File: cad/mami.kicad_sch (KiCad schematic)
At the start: 130 parts, among them J1 Conn_01x02_Pin, SW1 SW_Push, SW10 SW_Push, SW11 SW_Push, SW12 SW_Push, SW13 SW_Push, SW14 SW_Push, SW15 SW_Push, SW16 SW_Push, SW17 SW_Push, SW18 SW_Push, SW19 SW_Push, SW2 SW_Push, SW20 SW_Push, SW21 SW_Push, SW22 SW_Push, SW23 SW_Push, SW24 SW_Push, SW25 SW_Push, SW26 SW_Push, SW27 SW_Push, SW28 SW_Push, SW29 SW_Push, SW3 SW_Push, SW30 SW_Push, SW31 SW_Push, SW32 SW_Push, SW33 SW_Push, SW34 SW_Push, SW35 SW_Push, SW36 SW_Push, SW37 SW_Push, SW38 SW_Push, SW39 SW_Push, SW4 SW_Push, SW40 SW_Push, SW41 SW_Push, SW42 SW_Push, SW43 ResetSW, SW45 SW_SPDT, SW5 SW_Push, SW6 SW_Push, SW7 SW_Push, SW8 SW_Push, SW9 SW_Push, U1 nice_nano

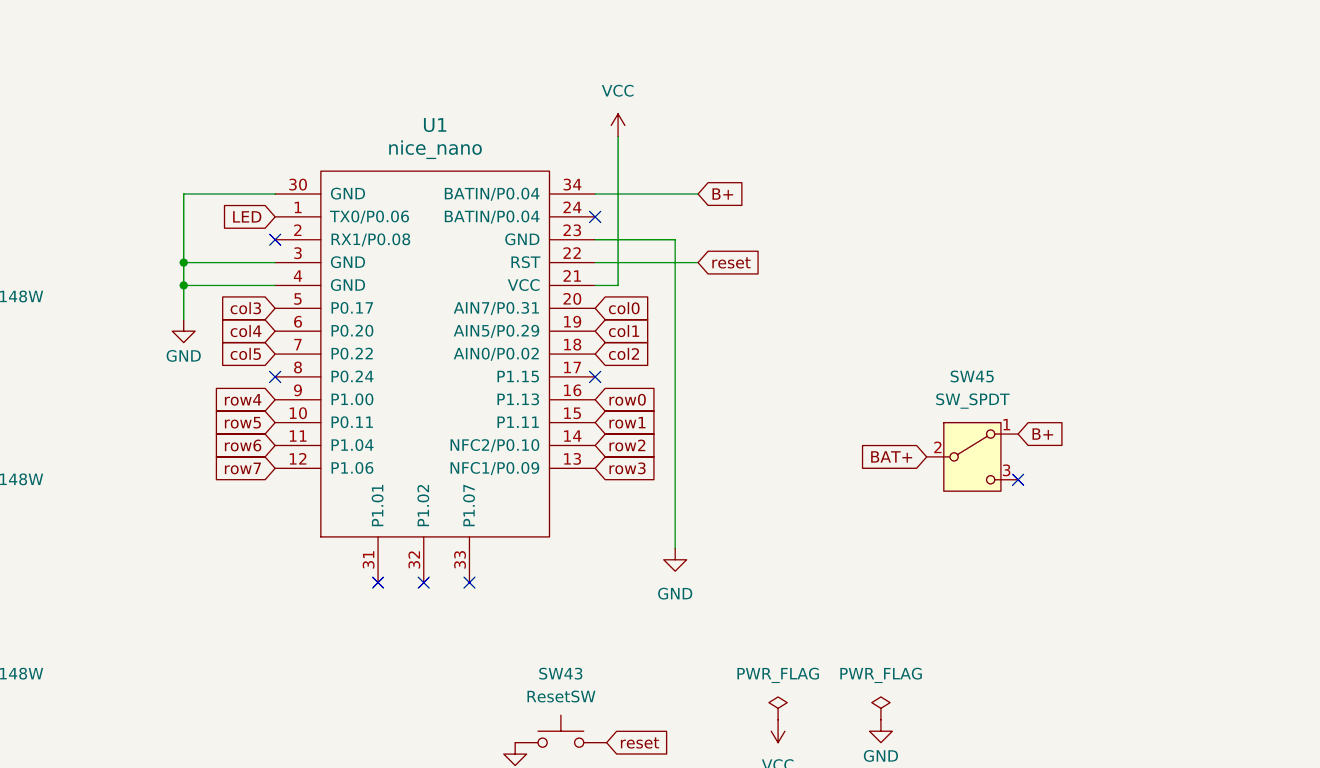
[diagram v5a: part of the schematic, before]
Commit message: ON/OFFスイッチを削除
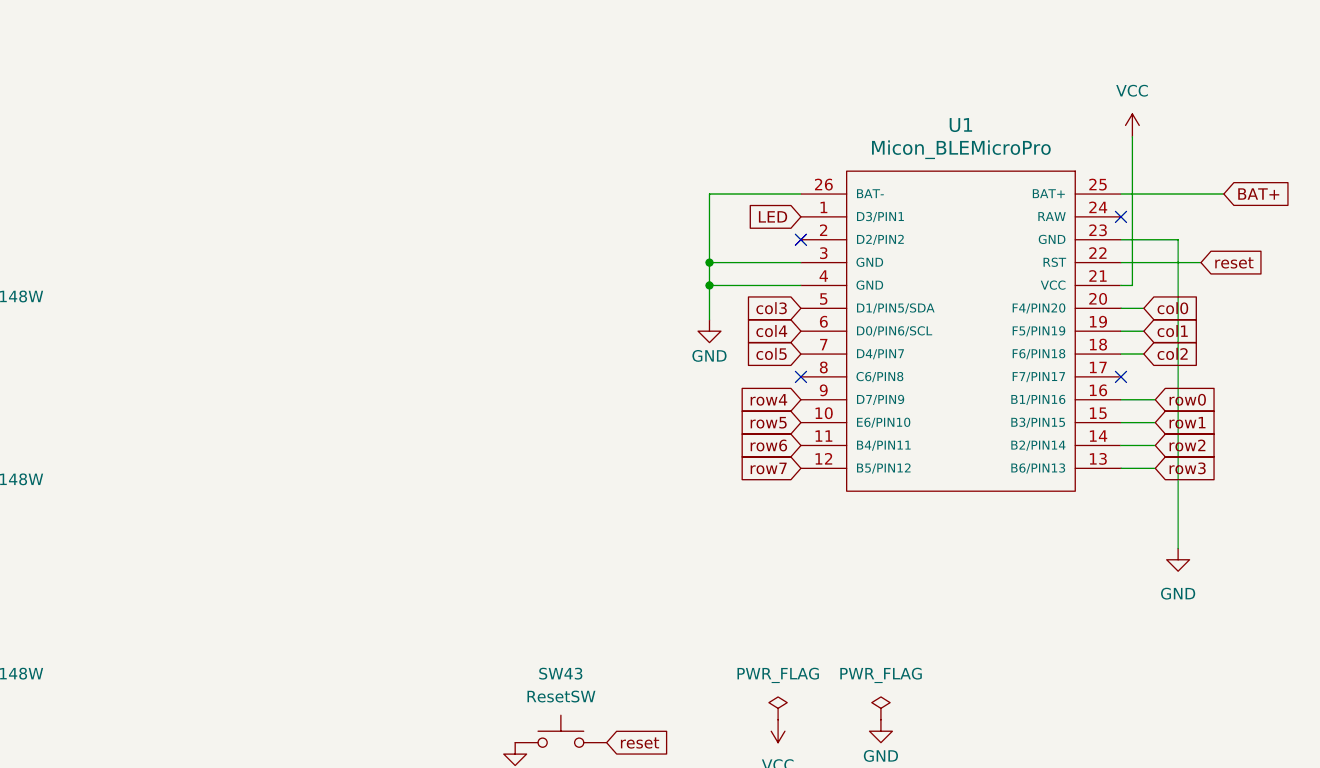
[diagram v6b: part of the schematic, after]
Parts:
- removed SW45: SW_SPDT, symbol Switch:SW_SPDT
- removed U1: nice_nano, symbol mylib:nice_nano
- added U1: Micon_BLEMicroPro, symbol salicylic:Micon_BLEMicroPro
- D43, D44, D45, D46, D47, D48, D49, D50, D51, D52, D53, D54, D55, D56, D57, D58, D59, D60, D61, D62, D63, D64, D65, D66, D67, D68, D69, D70, D71, D72, D73, D74, D75, D76, D77, D78, D79, D80, D81, D82, D83, D84: footprint LED_SMD:LED_SK6812MINI-E_3.2x2.8mm_P1.5mm_ReverseMount -> salicylic-3:LED_SK6812MINI-E_E
- J1: footprint (none) -> salicylic-3:Battery_BMP_2pin
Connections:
- net BAT+: now also U1.25 (BAT+)
- net GND: now also U1.23 (GND), U1.26 (BAT-), U1.3 (GND), U1.4 (GND)
- net LED: now also U1.1 (D3/PIN1)
- net VCC: now also U1.21 (VCC)
- net col0: now also U1.20 (F4/PIN20)
- net col1: now also U1.19 (F5/PIN19)
- net col2: now also U1.18 (F6/PIN18)
- net col3: now also U1.5 (D1/PIN5/SDA)
- net col4: now also U1.6 (D0/PIN6/SCL)
- net col5: now also U1.7 (D4/PIN7)
- net reset: now also U1.22 (RST)
- net row0: now also U1.16 (B1/PIN16)
- net row1: now also U1.15 (B3/PIN15)
- net row2: now also U1.14 (B2/PIN14)
- net row3: now also U1.13 (B6/PIN13)
- net row4: now also U1.9 (D7/PIN9)
- net row5: now also U1.10 (E6/PIN10)
- net row6: now also U1.11 (B4/PIN11)
- net row7: now also U1.12 (B5/PIN12)
- no-connect marks 9 -> 5

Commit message: reverse diode direction
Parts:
- D43, D44, D45, D46, D47, D48, D49, D50, D51, D52, D53, D54, D55, D56, D57, D58, D59, D60, D61, D62, D63, D64, D65, D66, D67, D68, D69, D70, D71, D72, D73, D74, D75, D76, D77, D78, D79, D80, D81, D82, D83, D84: footprint salicylic-3:LED_SK6812MINI-E_E -> Keebio-Parts:SK6812-MINI-E
- J1: footprint salicylic-3:Battery_BMP_2pin -> kbd-parts:Battery_BMP_2pin
- SW1, SW10, SW11, SW12, SW13, SW15, SW16, SW17, SW18, SW19, SW2, SW20, SW22, SW23, SW24, SW26, SW27, SW28, SW29, SW3, SW30, SW31, SW33, SW34, SW35, SW36, SW37, SW38, SW39, SW4, SW40, SW41, SW42, SW5, SW6, SW7, SW8, SW9: footprint kbd:keyswitch_cherrymx_hotswap_1u -> kbd-sw:CherryMX_Hotswap_1u
- SW14, SW32: footprint kbd:keyswitch_cherrymx_hotswap_1u -> kbd-sw:CherryMX_Hotswap_1.25u
- SW21, SW25: footprint kbd:keyswitch_cherrymx_hotswap_1u -> kbd-sw:CherryMX_Hotswap_2u
- U1: footprint (none) -> kbd-parts:Micon_BMP_7sKB
